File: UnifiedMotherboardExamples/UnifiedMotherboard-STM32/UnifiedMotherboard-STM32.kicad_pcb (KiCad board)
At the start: 2 copper layers, 22 x 25.1 mm, 1 part, among them U1 Unified Motherboard

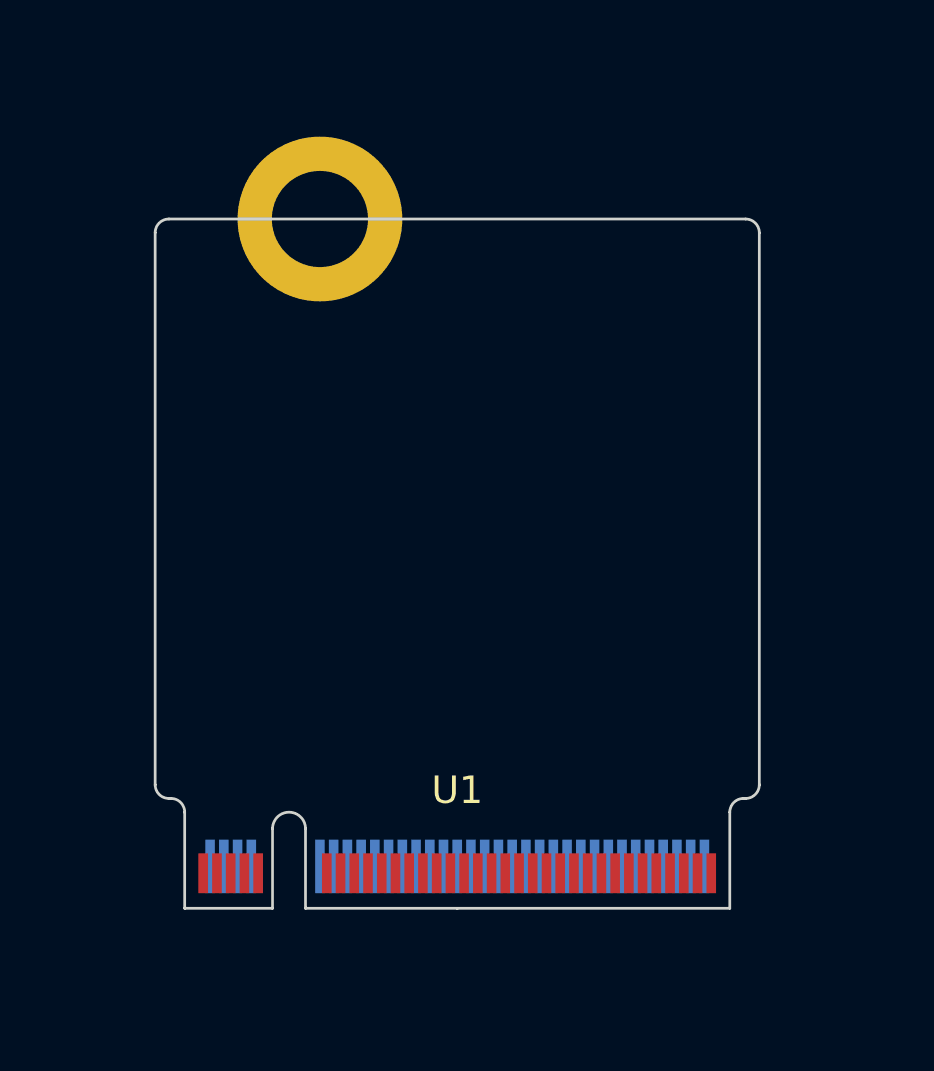
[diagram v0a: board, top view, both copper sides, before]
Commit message: Schematic for STM32F072 design
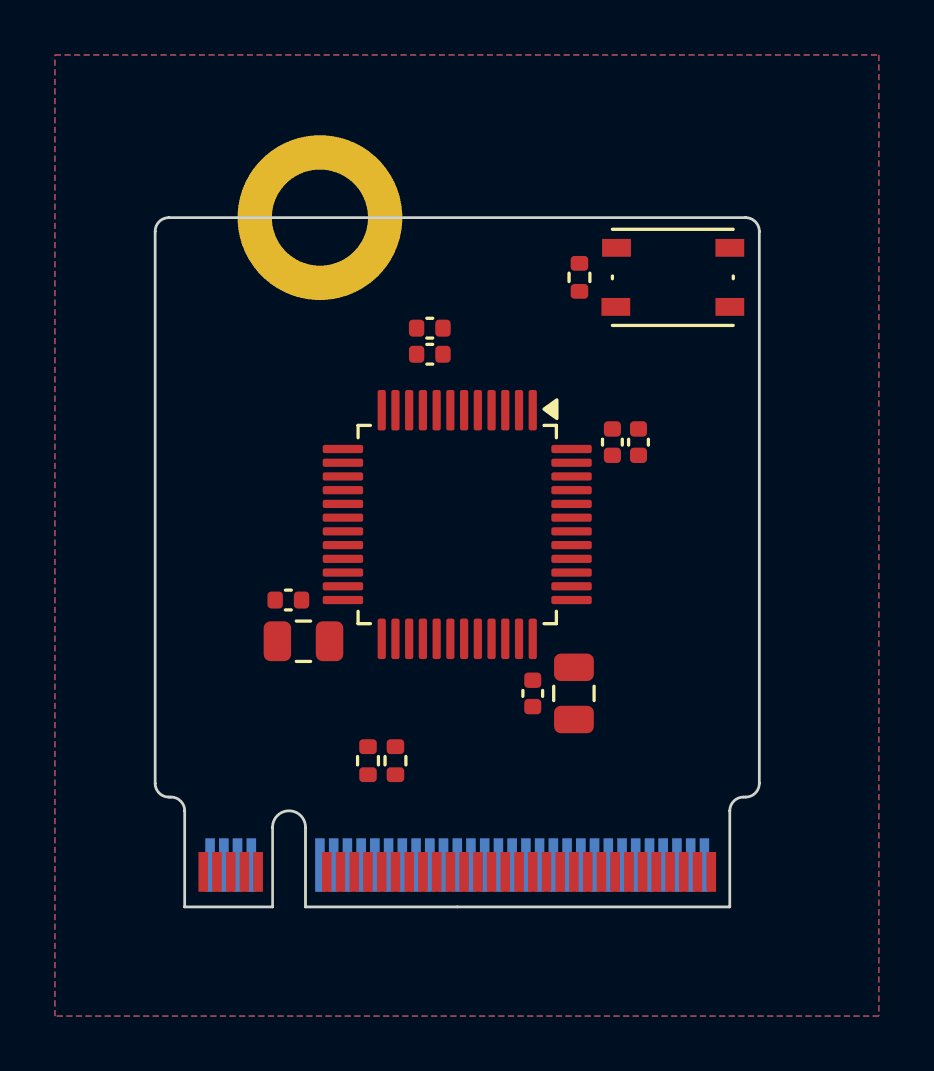
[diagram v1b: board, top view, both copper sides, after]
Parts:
- added C1: 100nF, Capacitor_SMD:C_0402_1005Metric, F.Cu at (196.2, 84.1)
- added C2: 100nF, Capacitor_SMD:C_0402_1005Metric, F.Cu at (195.3, 84.1)
- added C3: 100nF, Capacitor_SMD:C_0402_1005Metric, F.Cu at (183.5, 89.8)
- added C4: 4.7uF, Capacitor_SMD:C_0805_2012Metric, F.Cu at (184.1, 91.3)
- added C5: 4.7uF, Capacitor_SMD:C_0805_2012Metric, F.Cu at (193.9, 93.2)
- added C6: 100nF, Capacitor_SMD:C_0402_1005Metric, F.Cu at (192.4, 93.2)
- added C7: 1uF, Capacitor_SMD:C_0402_1005Metric, F.Cu at (188.7, 80.0)
- added C8: 10nF, Capacitor_SMD:C_0402_1005Metric, F.Cu at (188.7, 80.9)
- added R1: 10kR, Resistor_SMD:R_0402_1005Metric, F.Cu at (194.1, 78.1)
- added R2: 10kR, Resistor_SMD:R_0402_1005Metric, F.Cu at (187.4, 95.7)
- added R3: 10kR, Resistor_SMD:R_0402_1005Metric, F.Cu at (186.4, 95.7)
- added SW1: SW_Push, Button_Switch_SMD:SW_Push_1P1T_NO_Vertical_Wuerth_434133025816, F.Cu at (197.5, 78.1)
- added U2: STM32F072C8Tx, Package_QFP:LQFP-48_7x7mm_P0.5mm, F.Cu at (189.7, 87.1)
- U1: footprint UnifiedMotherBoard-Connector_PCBEdge:NGFF_M -> UnifiedMotherBoard-Connector_PCBEdge:UnifiedMotherboard
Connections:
- net Net-(U1-GND-Pad10) renamed GND
- U1 pad 1: Net-(U1-VBAT-Pad1) -> unconnected-(U1-VBAT-Pad1)
- U1 pad 11: unconnected-(U1-VDDA-Pad11) -> VDDA
- U1 pad 12: Net-(U1-VBUS-Pad12) -> unconnected-(U1-VBUS-Pad12)
- U1 pad 14: Net-(U1-VBUS-Pad12) -> unconnected-(U1-VBUS-Pad12)_0
- U1 pad 15: unconnected-(U1-D44/A7-Pad15) -> /SWDIO
- U1 pad 17: unconnected-(U1-D43/A6-Pad17) -> /SWCLK
- U1 pad 18: unconnected-(U1-SCL-Pad18) -> /SCL
- U1 pad 19: unconnected-(U1-D42/A5-Pad19) -> /~{RESET}
- U1 pad 20: unconnected-(U1-SDA-Pad20) -> /SDA
- U1 pad 21: unconnected-(U1-D41/A4-Pad21) -> /D41/A7
- U1 pad 23: unconnected-(U1-D40/A3-Pad23) -> /D40/A6
- U1 pad 24: unconnected-(U1-SCLK-Pad24) -> /SCLK
- U1 pad 25: unconnected-(U1-D39/A2-Pad25) -> /D39/A5
- U1 pad 26: unconnected-(U1-MOSI-Pad26) -> /MOSI
- U1 pad 27: unconnected-(U1-D38/A1-Pad27) -> /D38/A4
- U1 pad 28: unconnected-(U1-MISO-Pad28) -> /MISO
- U1 pad 29: unconnected-(U1-D37/A0-Pad29) -> /D37/A3
- U1 pad 3: Net-(U1-VBAT-Pad1) -> unconnected-(U1-VBAT-Pad1)_0
- U1 pad 30: unconnected-(U1-~{CS}-Pad30) -> /~{CS}
- U1 pad 31: unconnected-(U1-D18-Pad31) -> /D18
- U1 pad 32: unconnected-(U1-D36-Pad32) -> /D36/A2
- U1 pad 33: unconnected-(U1-D17-Pad33) -> /D17
- U1 pad 34: unconnected-(U1-D35-Pad34) -> /D35/A1
- U1 pad 35: unconnected-(U1-D16-Pad35) -> /D16
- U1 pad 36: unconnected-(U1-D34-Pad36) -> /D34/A0
- U1 pad 37: unconnected-(U1-D15-Pad37) -> /D15
- U1 pad 38: unconnected-(U1-D33-Pad38) -> /D33
- U1 pad 39: unconnected-(U1-D14-Pad39) -> /D14
- U1 pad 4: unconnected-(U1-D+-Pad4) -> /USB_D+
- U1 pad 40: unconnected-(U1-D32-Pad40) -> /D32
- U1 pad 41: unconnected-(U1-D13-Pad41) -> /D13
- U1 pad 42: unconnected-(U1-D31-Pad42) -> /D31
- U1 pad 43: unconnected-(U1-D12-Pad43) -> /D12
- U1 pad 44: unconnected-(U1-D30-Pad44) -> /D30
- U1 pad 45: unconnected-(U1-D11-Pad45) -> /D11
- U1 pad 46: unconnected-(U1-D29-Pad46) -> /D29
- U1 pad 47: unconnected-(U1-D10-Pad47) -> /D10
- U1 pad 48: unconnected-(U1-D28-Pad48) -> /D28
- U1 pad 49: unconnected-(U1-D9-Pad49) -> /D9
- U1 pad 50: unconnected-(U1-D27-Pad50) -> /D27
- U1 pad 51: unconnected-(U1-D8-Pad51) -> /D8
- U1 pad 52: unconnected-(U1-D26-Pad52) -> /D26
- U1 pad 53: unconnected-(U1-D7-Pad53) -> /D7
- U1 pad 54: unconnected-(U1-D25-Pad54) -> /D25
- U1 pad 55: unconnected-(U1-D6-Pad55) -> /D6
- U1 pad 56: unconnected-(U1-D24-Pad56) -> /D24
- U1 pad 57: unconnected-(U1-D5-Pad57) -> /D5
- U1 pad 58: unconnected-(U1-D23-Pad58) -> /D23
- U1 pad 59: unconnected-(U1-D4-Pad59) -> /D4
- U1 pad 6: unconnected-(U1-D--Pad6) -> /USB_D-
- U1 pad 60: unconnected-(U1-D22-Pad60) -> /D22
- U1 pad 61: unconnected-(U1-D3-Pad61) -> /D3
- U1 pad 62: unconnected-(U1-D21-Pad62) -> /D21
- U1 pad 63: unconnected-(U1-D2-Pad63) -> /D2
- U1 pad 64: unconnected-(U1-D20-Pad64) -> /D20
- U1 pad 65: unconnected-(U1-D1-Pad65) -> /D1
- U1 pad 66: unconnected-(U1-D19-Pad66) -> /D19
- U1 pad 67: unconnected-(U1-D0-Pad67) -> /D0
- U1 pad 9: unconnected-(U1-VCC-Pad9) -> VDD
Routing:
- added copper zone on B.Cu, net GND
- added copper zone on F.Cu, net GND
- added copper zone on In1.Cu, net GND
- added copper zone on In2.Cu, net VDD
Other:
- copper layers 2 -> 4
